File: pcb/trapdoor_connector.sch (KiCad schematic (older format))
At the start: 3 parts

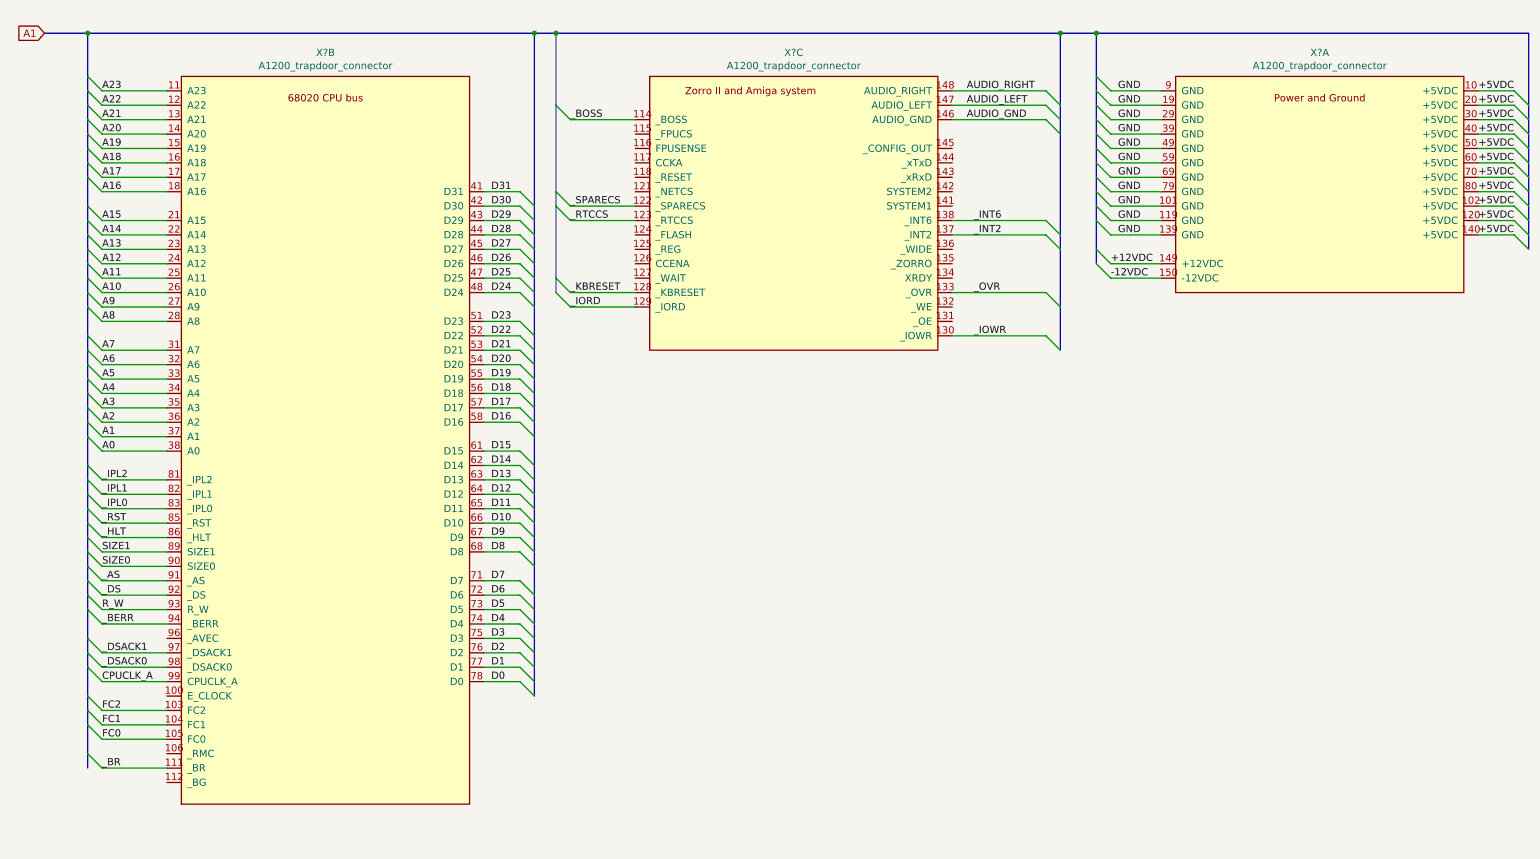
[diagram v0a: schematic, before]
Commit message: hierarchy updated
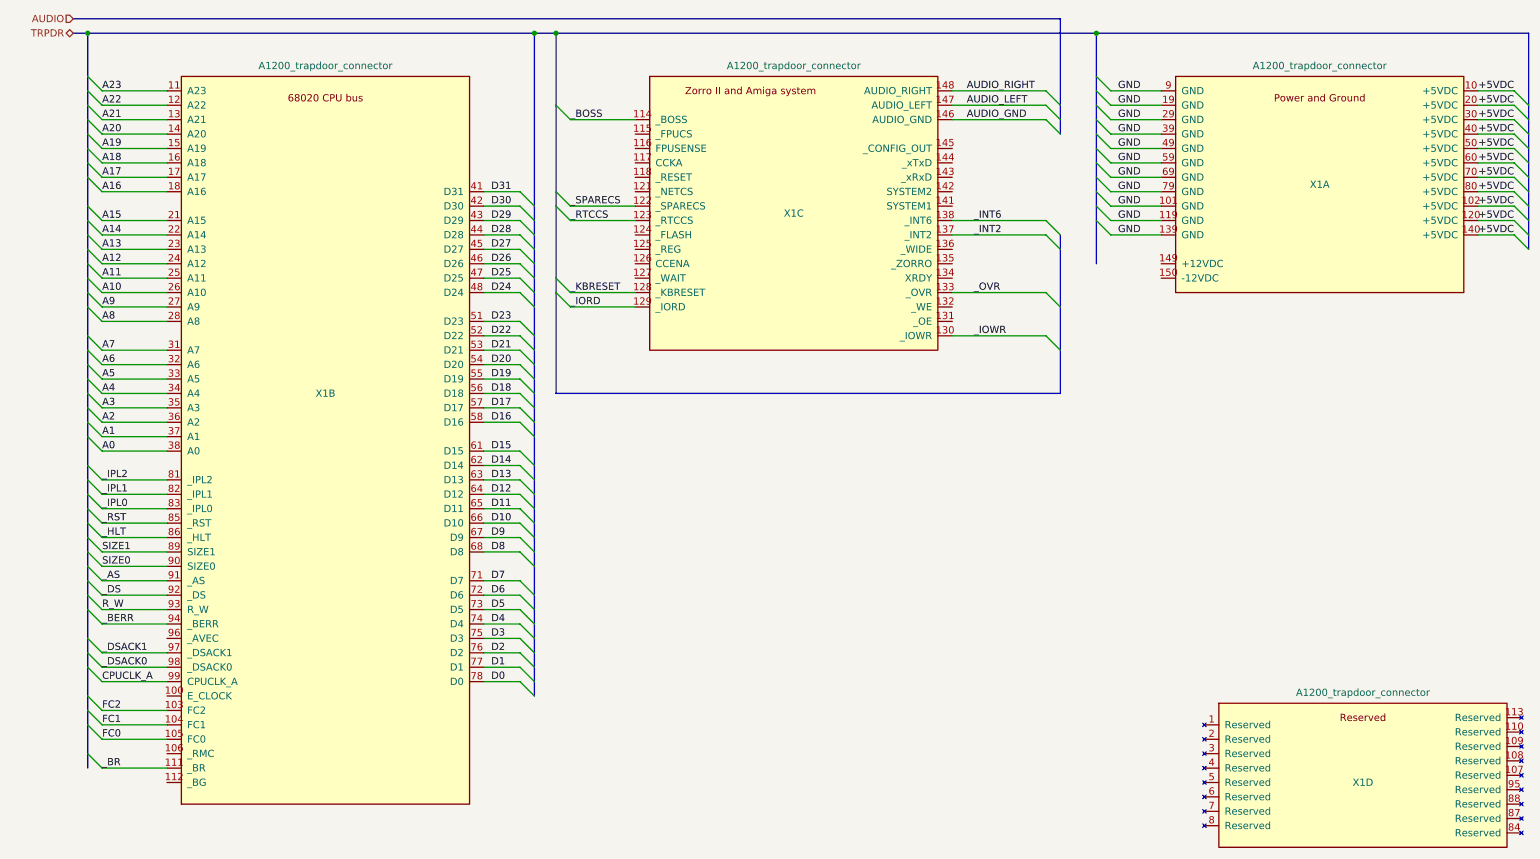
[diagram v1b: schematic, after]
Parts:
- added unit 4 of X1
- gave numbers to parts that had none: 1
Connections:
- net +12VDC: no longer names the net of X1.149 (+12VDC)
- net -12VDC: no longer names the net of X1.150 (-12VDC)
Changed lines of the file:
@@
 $Descr A4 11693 8268
 encoding utf-8
-Sheet 2 2
+Sheet 2 10
 Title "WishMaster 1200"
 Date ""
@@
 Comment4 ""
 $EndDescr
-Text GLabel 700  700  0    50   Input ~ 0
-A1
 $Comp
-L WM1200:A1200_trapdoor_connector X?
-U 1 1 5E62B199
-P 9550 2500
-F 0 "X?" H 9550 4165 50  0000 C CNN
-F 1 "A1200_trapdoor_connector" H 9550 4074 50  0000 C CNN
-F 2 "" H 9500 2500 50  0001 C CNN
-F 3 "" H 9500 2500 50  0001 C CNN
-	1    9550 2500
-	1    0    0    -1
-$EndComp
-$Comp
-L WM1200:A1200_trapdoor_connector X?
+L WM1200:A1200_trapdoor_connector X1
 U 3 1 5E6527FA
 P 5900 2900
-F 0 "X?" H 5900 4965 50  0000 C CNN
+F 0 "X1" H 5900 3850 50  0000 C CNN
 F 1 "A1200_trapdoor_connector" H 5900 4874 50  0000 C CNN
 F 2 "" H 5850 2900 50  0001 C CNN
@@
 $EndComp
 Wire Bus Line
-	700  700  1000 700
+	900  700  1000 700
 Connection ~ 1000 700
 Wire Bus Line
@@
 	1550 5400 1100 5400
 $Comp
-L WM1200:A1200_trapdoor_connector X?
+L WM1200:A1200_trapdoor_connector X1
 U 2 1 5E64CEB2
 P 2650 6050
-F 0 "X?" H 2650 11265 50  0000 C CNN
+F 0 "X1" H 2650 8900 50  0000 C CNN
 F 1 "A1200_trapdoor_connector" H 2650 11174 50  0000 C CNN
 F 2 "" H 2600 6050 50  0001 C CNN
@@
 Text Label 3800 5200 0    50   ~ 0
 D0
-Entry Wire Line
-	8000 1000 8100 1100
-Entry Wire Line
-	8000 1100 8100 1200
-Entry Wire Line
-	8000 1200 8100 1300
-Entry Wire Line
-	8000 1300 8100 1400
-Entry Wire Line
-	8000 1400 8100 1500
-Entry Wire Line
-	8000 1600 8100 1700
-Entry Wire Line
-	8000 1700 8100 1800
-Entry Wire Line
-	8000 1800 8100 1900
-Entry Wire Line
-	8000 1900 8100 2000
-Entry Wire Line
-	8000 2000 8100 2100
-Entry Wire Line
-	8000 2200 8100 2300
-Entry Wire Line
-	8000 2300 8100 2400
-Entry Wire Line
-	10900 1100 11000 1200
-Entry Wire Line
-	10900 1200 11000 1300
-Entry Wire Line
-	10900 1300 11000 1400
-Entry Wire Line
-	10900 1400 11000 1500
-Entry Wire Line
-	10900 1500 11000 1600
-Entry Wire Line
-	10900 1600 11000 1700
-Entry Wire Line
-	10900 1700 11000 1800
-Entry Wire Line
-	10900 1800 11000 1900
-Entry Wire Line
-	10900 1900 11000 2000
-Entry Wire Line
-	10900 2000 11000 2100
-Entry Wire Line
-	10900 2100 11000 2200
 Wire Wire Line
 	3750 1800 4000 1800
@@
 	4000 5200 3750 5200
 Connection ~ 4250 700
-Wire Bus Line
-	4250 700  7750 700
-Connection ~ 7750 700
-Wire Bus Line
-	7750 700  8000 700
-Connection ~ 8000 700
-Wire Bus Line
-	8000 700  11000 700
 Entry Wire Line
 	4250 1200 4350 1300
@@
 Wire Wire Line
 	7000 2800 7650 2800
-Wire Wire Line
-	8100 1100 8450 1100
-Wire Wire Line
-	8450 1200 8100 1200
-Wire Wire Line
-	8100 1300 8450 1300
-Wire Wire Line
-	8450 1400 8100 1400
-Wire Wire Line
-	8100 1500 8450 1500
-Wire Wire Line
-	8100 1700 8450 1700
-Wire Wire Line
-	8450 1800 8100 1800
-Wire Wire Line
-	8100 1900 8450 1900
-Wire Wire Line
-	8450 2000 8100 2000
-Wire Wire Line
-	8100 2100 8450 2100
-Wire Wire Line
-	8100 2300 8450 2300
-Wire Wire Line
-	8450 2400 8100 2400
-Wire Wire Line
-	10650 1100 10900 1100
-Wire Wire Line
-	10900 1200 10650 1200
-Wire Wire Line
-	10650 1300 10900 1300
-Wire Wire Line
-	10900 1400 10650 1400
-Wire Wire Line
-	10650 1500 10900 1500
-Wire Wire Line
-	10900 1600 10650 1600
-Wire Wire Line
-	10650 1700 10900 1700
-Wire Wire Line
-	10900 1800 10650 1800
-Wire Wire Line
-	10650 1900 10900 1900
-Wire Wire Line
-	10900 2000 10650 2000
-Wire Wire Line
-	10650 2100 10900 2100
-Entry Wire Line
-	8000 1500 8100 1600
-Wire Wire Line
-	8100 1600 8450 1600
-Text Label 8150 1100 0    50   ~ 0
-GND
-Text Label 8150 1200 0    50   ~ 0
-GND
-Text Label 8150 1300 0    50   ~ 0
-GND
-Text Label 8150 1400 0    50   ~ 0
-GND
-Text Label 8150 1500 0    50   ~ 0
-GND
-Text Label 8150 1600 0    50   ~ 0
-GND
-Text Label 8150 1700 0    50   ~ 0
-GND
-Text Label 8150 1800 0    50   ~ 0
-GND
-Text Label 8150 1900 0    50   ~ 0
-GND
-Text Label 8150 2000 0    50   ~ 0
-GND
-Text Label 8150 2100 0    50   ~ 0
-GND
-Text Label 10650 1100 0    50   ~ 0
-+5VDC
-Text Label 10650 1200 0    50   ~ 0
-+5VDC
-Text Label 10650 1300 0    50   ~ 0
-+5VDC
-Text Label 10650 1400 0    50   ~ 0
-+5VDC
-Text Label 10650 1500 0    50   ~ 0
-+5VDC
-Text Label 10650 1600 0    50   ~ 0
-+5VDC
-Text Label 10650 1800 0    50   ~ 0
-+5VDC
-Text Label 10650 1700 0    50   ~ 0
-+5VDC
-Text Label 10650 1900 0    50   ~ 0
-+5VDC
-Text Label 10650 2000 0    50   ~ 0
-+5VDC
-Text Label 10650 2100 0    50   ~ 0
-+5VDC
-Text Label 8100 2300 0    50   ~ 0
-+12VDC
-Text Label 8100 2400 0    50   ~ 0
--12VDC
 Text Label 4350 1300 0    50   ~ 0
 _BOSS
@@
 Text Label 7150 2800 0    50   ~ 0
 _IOWR
-Wire Bus Line
-	4250 700  4250 2500
-Wire Bus Line
-	7750 700  7750 2900
+$Comp
+L WM1200:A1200_trapdoor_connector X1
+U 4 1 5E55669B
+P 9850 6350
+F 0 "X1" H 9850 6800 50  0000 C CNN
+F 1 "A1200_trapdoor_connector" H 9850 7424 50  0000 C CNN
+F 2 "" H 9800 6350 50  0001 C CNN
+F 3 "" H 9800 6350 50  0001 C CNN
+	4    9850 6350
+	1    0    0    -1
+$EndComp
+Text HLabel 900  700  0    50   BiDi ~ 0
+TRPDR
+Text Label 10650 2100 0    50   ~ 0
++5VDC
+Text Label 10650 2000 0    50   ~ 0
++5VDC
+Text Label 10650 1900 0    50   ~ 0
++5VDC
+Text Label 10650 1700 0    50   ~ 0
++5VDC
+Text Label 10650 1800 0    50   ~ 0
++5VDC
+Text Label 10650 1600 0    50   ~ 0
++5VDC
+Text Label 10650 1500 0    50   ~ 0
++5VDC
+Text Label 10650 1400 0    50   ~ 0
++5VDC
+Text Label 10650 1300 0    50   ~ 0
++5VDC
+Text Label 10650 1200 0    50   ~ 0
++5VDC
+Text Label 10650 1100 0    50   ~ 0
++5VDC
+Text Label 8150 2100 0    50   ~ 0
+GND
+Text Label 8150 2000 0    50   ~ 0
+GND
+Text Label 8150 1900 0    50   ~ 0
+GND
+Text Label 8150 1800 0    50   ~ 0
+GND
+Text Label 8150 1700 0    50   ~ 0
+GND
+Text Label 8150 1600 0    50   ~ 0
+GND
+Text Label 8150 1500 0    50   ~ 0
+GND
+Text Label 8150 1400 0    50   ~ 0
+GND
+Text Label 8150 1300 0    50   ~ 0
+GND
+Text Label 8150 1200 0    50   ~ 0
+GND
+Text Label 8150 1100 0    50   ~ 0
+GND
+Wire Wire Line
+	8100 1600 8450 1600
+Entry Wire Line
+	8000 1500 8100 1600
+Wire Wire Line
+	10650 2100 10900 2100
+Wire Wire Line
+	10900 2000 10650 2000
+Wire Wire Line
+	10650 1900 10900 1900
+Wire Wire Line
+	10900 1800 10650 1800
+Wire Wire Line
+	10650 1700 10900 1700
+Wire Wire Line
+	10900 1600 10650 1600
+Wire Wire Line
+	10650 1500 10900 1500
+Wire Wire Line
+	10900 1400 10650 1400
+Wire Wire Line
+	10650 1300 10900 1300
+Wire Wire Line
+	10900 1200 10650 1200
+Wire Wire Line
+	10650 1100 10900 1100
+Wire Wire Line
+	8100 2100 8450 2100
+Wire Wire Line
+	8450 2000 8100 2000
+Wire Wire Line
+	8100 1900 8450 1900
+Wire Wire Line
+	8450 1800 8100 1800
+Wire Wire Line
+	8100 1700 8450 1700
+Wire Wire Line
+	8100 1500 8450 1500
+Wire Wire Line
+	8450 1400 8100 1400
+Wire Wire Line
+	8100 1300 8450 1300
+Wire Wire Line
+	8450 1200 8100 1200
+Wire Wire Line
+	8100 1100 8450 1100
+Wire Bus Line
+	8000 700  11000 700
+Entry Wire Line
+	10900 2100 11000 2200
+Entry Wire Line
+	10900 2000 11000 2100
+Entry Wire Line
+	10900 1900 11000 2000
+Entry Wire Line
+	10900 1800 11000 1900
+Entry Wire Line
+	10900 1700 11000 1800
+Entry Wire Line
+	10900 1600 11000 1700
+Entry Wire Line
+	10900 1500 11000 1600
+Entry Wire Line
+	10900 1400 11000 1500
+Entry Wire Line
+	10900 1300 11000 1400
+Entry Wire Line
+	10900 1200 11000 1300
+Entry Wire Line
+	10900 1100 11000 1200
+Entry Wire Line
+	8000 2000 8100 2100
+Entry Wire Line
+	8000 1900 8100 2000
+Entry Wire Line
+	8000 1800 8100 1900
+Entry Wire Line
+	8000 1700 8100 1800
+Entry Wire Line
+	8000 1600 8100 1700
+Entry Wire Line
+	8000 1400 8100 1500
+Entry Wire Line
+	8000 1300 8100 1400
+Entry Wire Line
+	8000 1200 8100 1300
+Entry Wire Line
+	8000 1100 8100 1200
+Entry Wire Line
+	8000 1000 8100 1100
+$Comp
+L WM1200:A1200_trapdoor_connector X1
+U 1 1 5E62B199
+P 9550 2500
+F 0 "X1" H 9550 3250 50  0000 C CNN
+F 1 "A1200_trapdoor_connector" H 9550 4074 50  0000 C CNN
+F 2 "" H 9500 2500 50  0001 C CNN
+F 3 "" H 9500 2500 50  0001 C CNN
+	1    9550 2500
+	1    0    0    -1
+$EndComp
+Connection ~ 8000 700
+Wire Bus Line
+	4250 3200 7750 3200
+Wire Bus Line
+	4250 700  8000 700
+Wire Bus Line
+	7750 600  900  600
+Text HLabel 900  600  0    50   Input ~ 0
+AUDIO
+Wire Bus Line
+	7750 600  7750 1400
+Wire Bus Line
+	7750 2100 7750 3200
+Wire Bus Line
+	4250 700  4250 3200
 Wire Bus Line
 	11000 700  11000 2200

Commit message: some work on sheets
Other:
- moved on the sheet: X1A, X1C
